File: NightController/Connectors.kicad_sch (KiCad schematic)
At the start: 2 parts, among them J201 Conn_02x20_Odd_Even, J202 Conn_02x20_Odd_Even

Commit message: Working on schematic
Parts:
- added J701: Conn_01x02_Socket, symbol Connector:Conn_01x02_Socket
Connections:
- net GND: now also J701.2 (Pin_2)
- new net BAT_BAT: J701.1 (Pin_1)
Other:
- note added: "Connector for battery"
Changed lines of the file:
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@@
+	(wire
+		(pts
+			(xy 101.6 203.2) (xy 101.6 193.04)
+		)
+		(stroke
+			(width 0)
+			(type default)
+		)
+	)
 	(wire
 		(pts
@@
 	(wire
 		(pts
+			(xy 88.9 190.5) (xy 114.3 190.5)
+		)
+		(stroke
+			(width 0)
+			(type default)
+		)
+	)
+	(wire
+		(pts
 			(xy 88.9 74.93) (xy 95.25 74.93)
 		)
@@
 		(pts
 			(xy 127 115.57) (xy 120.65 115.57)
+		)
+		(stroke
+			(width 0)
+			(type default)
+		)
+	)
+	(wire
+		(pts
+			(xy 101.6 193.04) (xy 88.9 193.04)
 		)
 		(stroke
@@
 		)
 	)
+	(text "Connector for battery\n"
+		(exclude_from_sim no)
+		(at 76.2 176.784 0)
+		(effects
+			(font
+				(size 1.905 1.905)
+			)
+			(justify left)
+		)
+	)
 	(label "DIN"
 		(at 168.91 104.14 180)
@@
 		)
 	)
+	(label "BAT_BAT"
+		(at 97.79 190.5 0)
+		(fields_autoplaced yes)
+		(effects
+			(font
+				(size 1.27 1.27)
+			)
+			(justify left bottom)
+		)
+	)
 	(label "DOUT"
 		(at 168.91 101.6 180)
@@
 			)
 			(justify right bottom)
+		)
+	)
+	(hierarchical_label "BAT_BAT"
+		(shape input)
+		(at 114.3 190.5 0)
+		(fields_autoplaced yes)
+		(effects
+			(font
+				(size 1.27 1.27)
+			)
+			(justify left)
 		)
 	)
@@
 	)
 	(symbol
+		(lib_id "Connector:Conn_01x02_Socket")
+		(at 83.82 190.5 0)
+		(mirror y)
+		(unit 1)
+		(exclude_from_sim no)
+		(in_bom yes)
+		(on_board yes)
+		(dnp no)
+		(fields_autoplaced yes)
+		(property "Reference" "J701"
+			(at 84.455 185.42 0)
+			(effects
+				(font
+					(size 1.27 1.27)
+				)
+			)
+		)
+		(property "Value" "Conn_01x02_Socket"
+			(at 84.455 187.96 0)
+			(effects
+				(font
+					(size 1.27 1.27)
+				)
+			)
+		)
+		(property "Footprint" ""
+			(at 83.82 190.5 0)
+			(effects
+				(font
+					(size 1.27 1.27)
+				)
+				(hide yes)
+			)
+		)
+		(property "Datasheet" "~"
+			(at 83.82 190.5 0)
+			(effects
+				(font
+					(size 1.27 1.27)
+				)
+				(hide yes)
+			)
+		)
+		(property "Description" "Generic connector, single row, 01x02, script generated"
+			(at 83.82 190.5 0)
+			(effects
+				(font
+					(size 1.27 1.27)
+				)
+				(hide yes)
+			)
+		)
+		(pin "1"
+		)
+		(pin "2"
+		)
+		(instances
+			(project ""
+				(path "/84972824-c6a3-4762-8148-c4d5b5ede147/a4481730-1ede-45e2-bdc5-33913a30df4a"
+					(reference "J701")
+					(unit 1)
+				)
+			)
+		)
+	)
+	(symbol
 		(lib_id "power:GND")
 		(at 88.9 105.41 270)
@@
 					(unit 1)
 				)
+			)
+		)
+	)
+	(symbol
+		(lib_id "power:GND")
+		(at 101.6 203.2 0)
+		(unit 1)
+		(exclude_from_sim no)
+		(in_bom yes)
+		(on_board yes)
+		(dnp no)
+		(fields_autoplaced yes)
+		(property "Reference" "#PWR0701"
+			(at 101.6 209.55 0)
+			(effects
+				(font
+					(size 1.27 1.27)
+				)
+				(hide yes)
+			)
+		)
+		(property "Value" "GND"
+			(at 101.6 208.28 0)
+			(effects
+				(font
+					(size 1.27 1.27)
+				)
+			)
+		)
+		(property "Footprint" ""
+			(at 101.6 203.2 0)
+			(effects
+				(font
+					(size 1.27 1.27)
+				)
+				(hide yes)
+			)
+		)
+		(property "Datasheet" ""
+			(at 101.6 203.2 0)
+			(effects
+				(font
+					(size 1.27 1.27)
+				)
+				(hide yes)
+			)
+		)
+		(property "Description" "Power symbol creates a global label with name \"GND\" , ground"
+			(at 101.6 203.2 0)
+			(effects
+				(font
+					(size 1.27 1.27)
+				)
+				(hide yes)
+			)
+		)
+		(pin "1"
+		)
+		(instances
+			(project "NightController"
+				(path "/84972824-c6a3-4762-8148-c4d5b5ede147/a4481730-1ede-45e2-bdc5-33913a30df4a"
+					(reference "#PWR0701")
+					(unit 1)
+				)

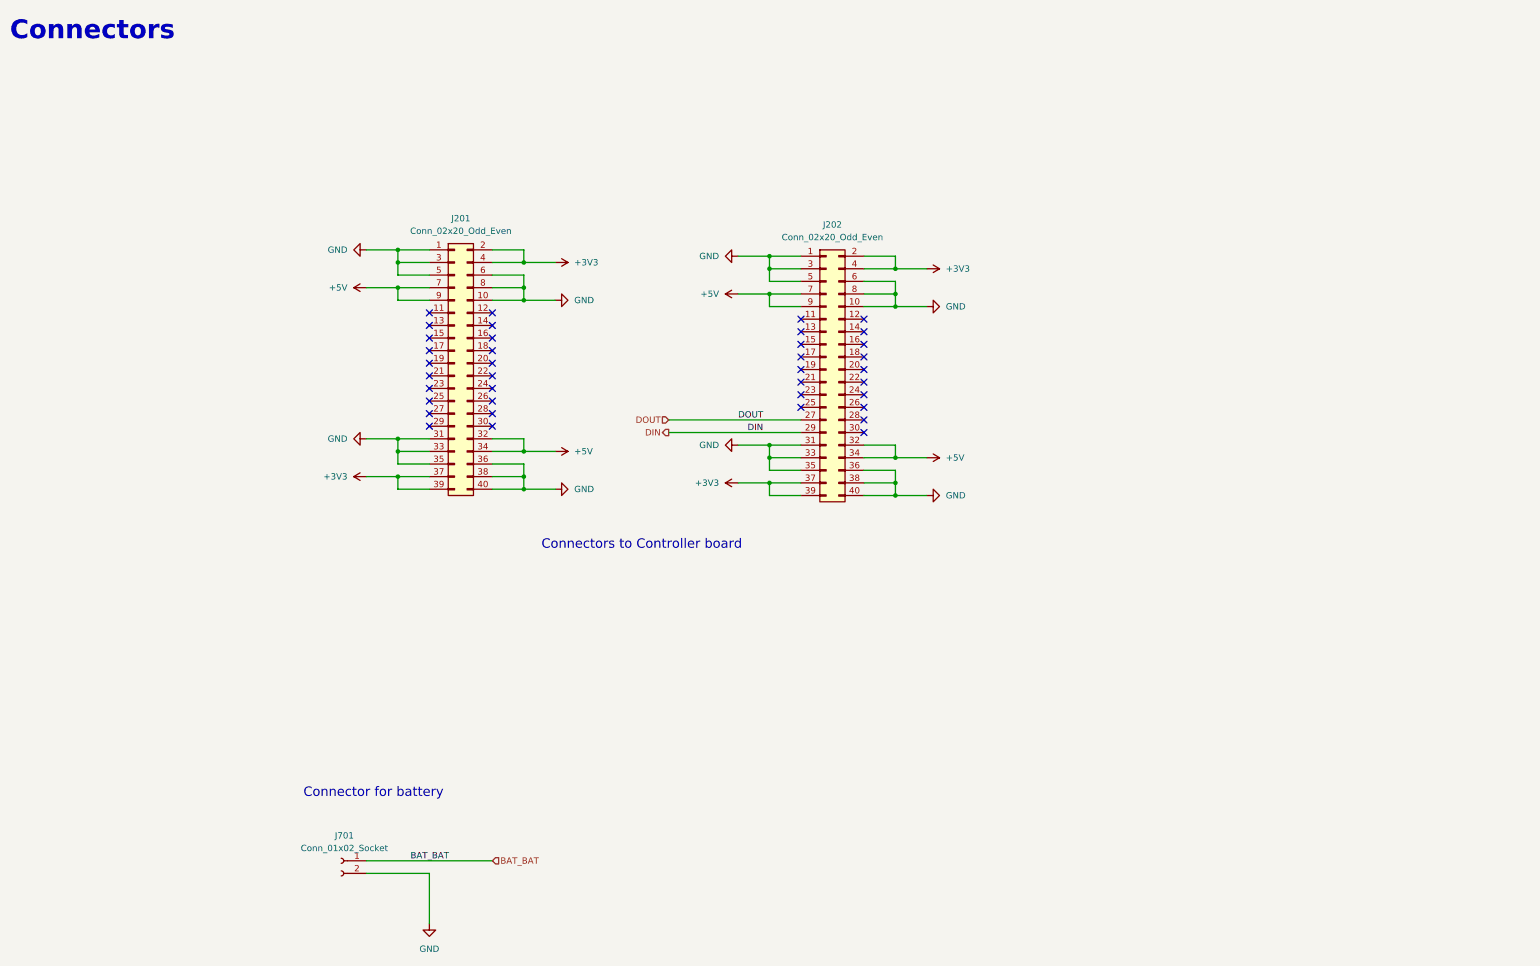
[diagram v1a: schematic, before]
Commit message: update schematic
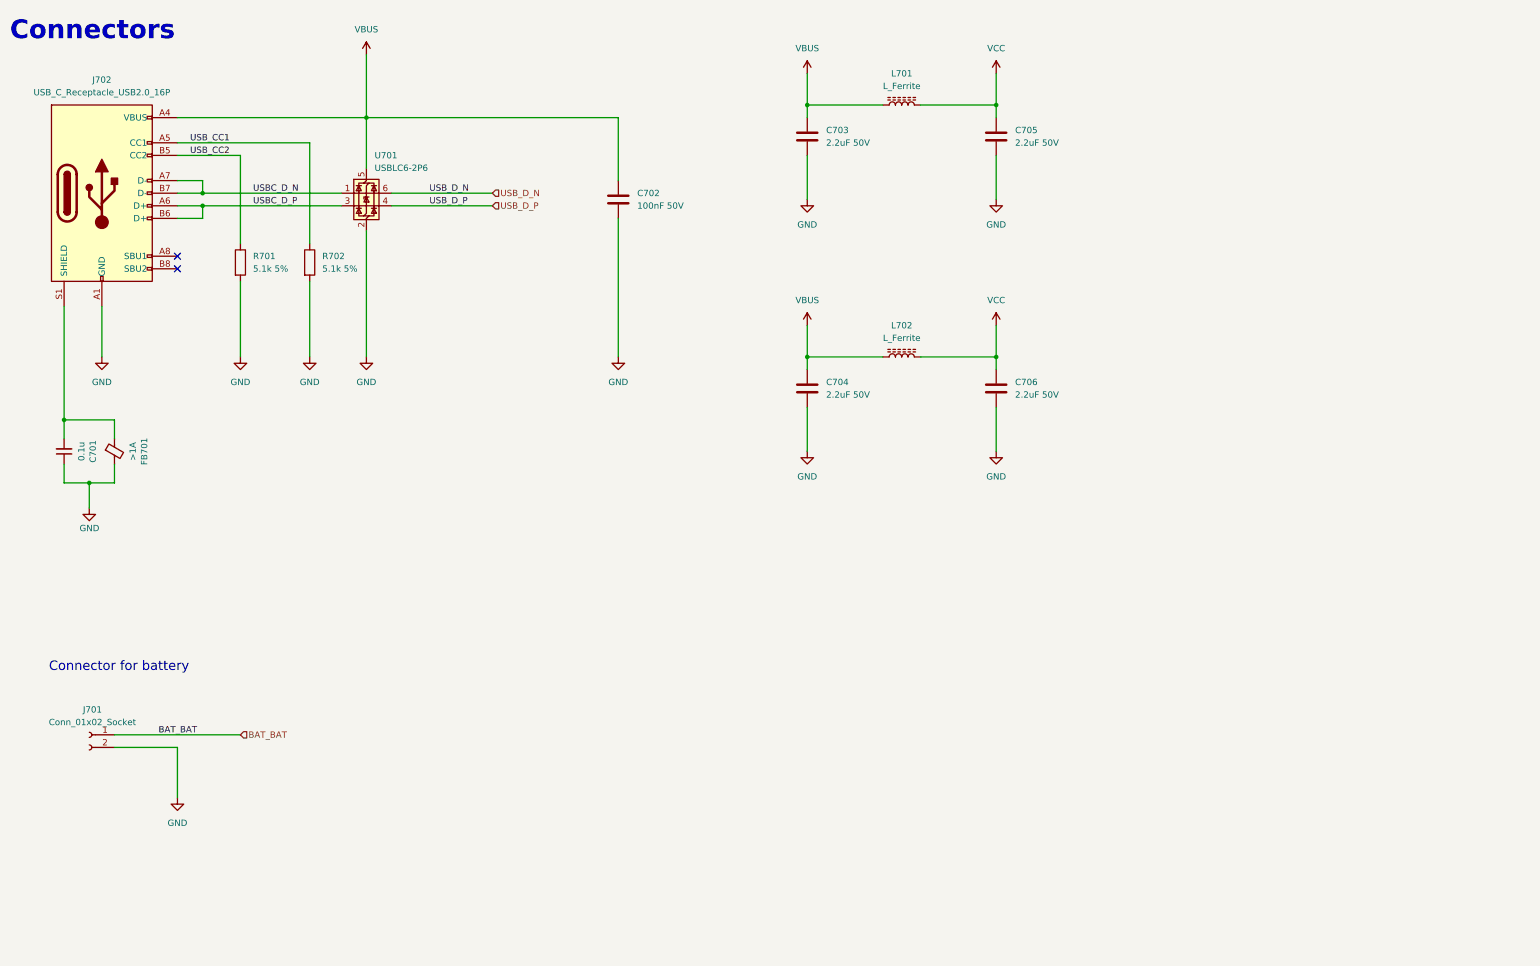
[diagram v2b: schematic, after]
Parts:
- removed J201, J202: Conn_02x20_Odd_Even, Connector_Molex:Molex_SlimStack_54722-0404_2x20_P0.50mm_Vertical, symbol Connector_Generic:Conn_02x20_Odd_Even
- added C701: 0.1u, Capacitor_SMD:C_0603_1608Metric, symbol Device:C_Small
- added C702: 100nF 50V, symbol Device:C
- added C703, C704, C705, C706: 2.2uF 50V, symbol Device:C
- added FB701: >1A, Inductor_SMD:L_0603_1608Metric, symbol Device:Ferrite_Bead_Small
- added J702: USB_C_Receptacle_USB2.0_16P, symbol Connector:USB_C_Receptacle_USB2.0_16P
- added L701, L702: L_Ferrite, symbol Device:L_Ferrite
- added R701, R702: 5.1k 5%, symbol Device:R
- added U701: USBLC6-2P6, Package_TO_SOT_SMD:SOT-666, symbol Power_Protection:USBLC6-2P6
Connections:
- net GND: now also C701.1, C702.2, C703.2, C704.2, C705.2, C706.2, FB701.2, J702.A1 (GND), J702.A12 (GND), J702.B1 (GND), J702.B12 (GND), R701.2, R702.2, U701.2 (GND)
- new net: C701.2, FB701.1, J702.S1 (SHIELD)
- new net USBC_D_N: J702.A7 (D-), J702.B7 (D-), U701.1 (I/O1)
- new net USBC_D_P: J702.A6 (D+), J702.B6 (D+), U701.3 (I/O2)
- new net USB_CC1: J702.A5 (CC1), R702.1
- new net USB_CC2: J702.B5 (CC2), R701.1
- new net USB_D_N: U701.6 (I/O1)
- new net USB_D_P: U701.4 (I/O2)
- new net VBUS: C702.1, C703.1, C704.1, J702.A4 (VBUS), J702.A9 (VBUS), J702.B4 (VBUS), J702.B9 (VBUS), L701.1, L702.1, U701.5 (VBUS)
- new net VCC: C705.1, C706.1, L701.2, L702.2
- no-connect marks 38 -> 2
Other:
- note removed: "Connectors to Controller board"
- moved on the sheet: J701

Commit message: Finished mcu
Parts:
- added Q601: 2N7002, Package_TO_SOT_SMD:SOT-23, symbol Transistor_FET:2N7002
- added R615: 10k 5%, symbol Device:R
- added R616: 1M 5%, symbol Device:R
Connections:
- net GND: now also Q601.2 (S), R616.1
- net VBUS: now also R615.1
- new net: Q601.1 (G), R615.2, R616.2
- new net USB_VBUS_SENS: Q601.3 (D)
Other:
- note added: "VBUS Sensing"
